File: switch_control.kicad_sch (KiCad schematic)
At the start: 16 parts, among them U10 74LVC1G86, U11 74LVC1G86, U26 74HC00, U27 74LVC1G32

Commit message: Multiplex clock I/O signals
- Allow switching of CLKIN and CLKOUT ports to trigger I/O and other signals
- Add SCT_CLK
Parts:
- U10, U11: Substitution (none) -> TI SN74LVC1G86DCKR
- U27: Substitution (none) -> TI SN74LVC1G32DCKR
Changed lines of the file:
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@@
 			)
 		)
-		(property "Datasheet" "http://www.ti.com/lit/sg/scyt129e/scyt129e.pdf"
+		(property "Datasheet" "https://www.umw-ic.com/static/pdf/f1fd48d5f9832d4f28de5af0ef559744.pdf"
 			(at 154.94 104.14 0)
 			(effects
@@
 		)
 		(property "Part Number" "SN74LVC1G32DCKR"
+			(at 154.94 104.14 0)
+			(effects
+				(font
+					(size 1.27 1.27)
+				)
+				(hide yes)
+			)
+		)
+		(property "Substitution" "TI SN74LVC1G32DCKR"
 			(at 154.94 104.14 0)
 			(effects
@@
 			)
 		)
-		(property "Datasheet" "http://www.ti.com/lit/sg/scyt129e/scyt129e.pdf"
+		(property "Datasheet" "https://www.umw-ic.com/static/pdf/7c3c8f547545258487a86f9b9a30ed55.pdf"
 			(at 154.94 54.61 0)
 			(effects
@@
 		)
 		(property "Part Number" "SN74LVC1G86DCKR"
+			(at 154.94 54.61 0)
+			(effects
+				(font
+					(size 1.27 1.27)
+				)
+				(hide yes)
+			)
+		)
+		(property "Substitution" "TI SN74LVC1G86DCKR"
 			(at 154.94 54.61 0)
 			(effects
@@
 			)
 		)
-		(property "Datasheet" "http://www.ti.com/lit/sg/scyt129e/scyt129e.pdf"
+		(property "Datasheet" "https://www.umw-ic.com/static/pdf/7c3c8f547545258487a86f9b9a30ed55.pdf"
 			(at 161.29 78.74 0)
 			(effects
@@
 			(at 161.29 78.74 0)
 			(effects
+				(font
+					(size 1.27 1.27)
+				)
+				(hide yes)
+			)
+		)
+		(property "Substitution" "TI SN74LVC1G86DCKR"
+			(at 161.29 78.74 0)
+			(effects

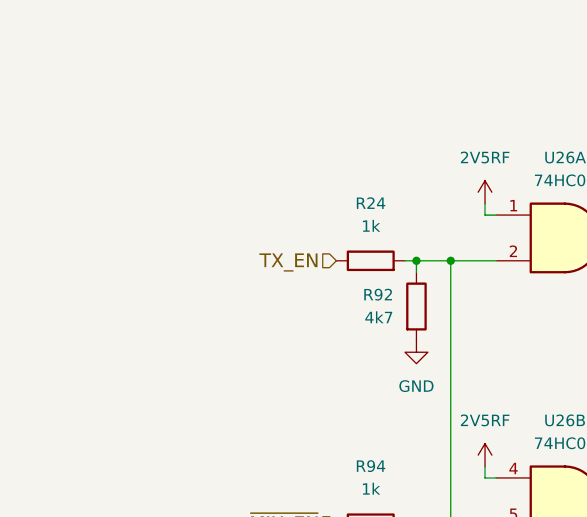
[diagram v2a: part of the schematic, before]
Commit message: Add TX_EN solder jumper
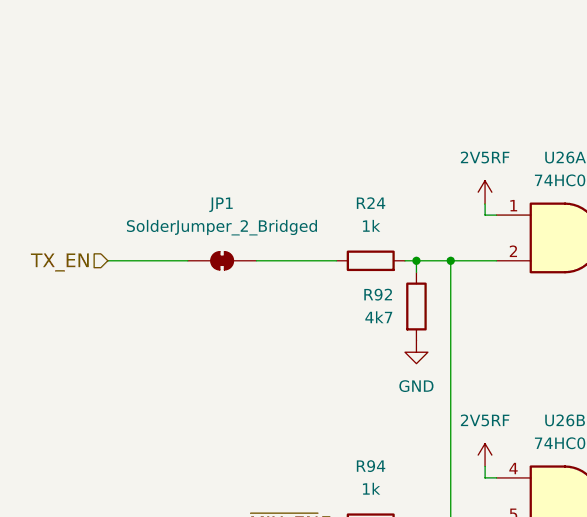
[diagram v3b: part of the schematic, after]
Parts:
- added JP1: SolderJumper_2_Bridged, Jumper:SolderJumper-2_P1.3mm_Bridged_RoundedPad1.0x1.5mm, symbol Jumper:SolderJumper_2_Bridged
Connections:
- net TX_EN: now also JP1.1 (A); no longer R24.1
- new net: JP1.2 (B), R24.1
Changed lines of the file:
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@@
+	(wire
+		(pts
+			(xy 66.04 54.61) (xy 74.93 54.61)
+		)
+		(stroke
+			(width 0)
+			(type default)
+		)
+	)
 	(wire
 		(pts
@@
 		(pts
 			(xy 173.99 34.29) (xy 128.27 34.29)
+		)
+		(stroke
+			(width 0)
+			(type default)
+		)
+	)
+	(wire
+		(pts
+			(xy 82.55 54.61) (xy 91.44 54.61)
 		)
 		(stroke
@@
 	(hierarchical_label "TX_EN"
 		(shape input)
-		(at 91.44 54.61 180)
+		(at 66.04 54.61 180)
 		(effects
 			(font
@@
 				)
 			)
+		)
+	)
+	(symbol
+		(lib_id "Jumper:SolderJumper_2_Bridged")
+		(at 78.74 54.61 0)
+		(unit 1)
+		(exclude_from_sim yes)
+		(in_bom no)
+		(on_board yes)
+		(dnp no)
+		(fields_autoplaced yes)
+		(property "Reference" "JP1"
+			(at 78.74 48.26 0)
+			(effects
+				(font
+					(size 1.27 1.27)
+				)
+			)
+		)
+		(property "Value" "SolderJumper_2_Bridged"
+			(at 78.74 50.8 0)
+			(effects
+				(font
+					(size 1.27 1.27)
+				)
+			)
+		)
+		(property "Footprint" "Jumper:SolderJumper-2_P1.3mm_Bridged_RoundedPad1.0x1.5mm"
+			(at 78.74 54.61 0)
+			(effects
+				(font
+					(size 1.27 1.27)
+				)
+				(hide yes)
+			)
+		)
+		(property "Datasheet" "~"
+			(at 78.74 54.61 0)
+			(effects
+				(font
+					(size 1.27 1.27)
+				)
+				(hide yes)
+			)
+		)
+		(property "Description" "Solder Jumper, 2-pole, closed/bridged"
+			(at 78.74 54.61 0)
+			(effects
+				(font
+					(size 1.27 1.27)
+				)
+				(hide yes)
+			)
+		)
+		(pin "2"
+		)
+		(pin "1"
+		)
+		(instances
+			(project ""
+				(path "/dba4afc6-760f-46cb-a936-032b76448f03/b52297f1-63c0-4931-9c57-b3b41fe2150b"
+					(reference "JP1")
+					(unit 1)
+				)
+			)

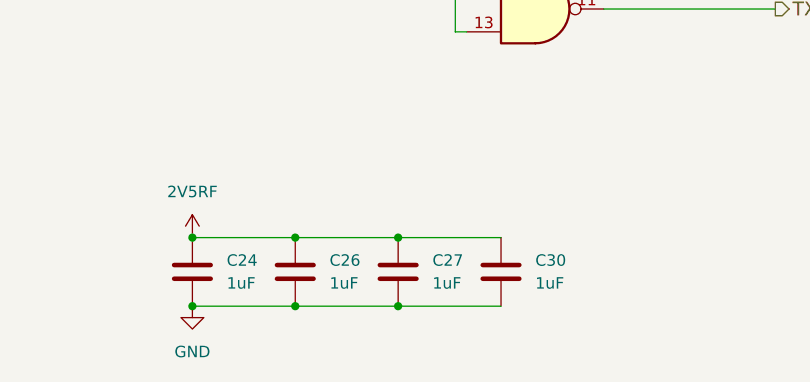
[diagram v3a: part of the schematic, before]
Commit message: Improve power supply filtering and decoupling
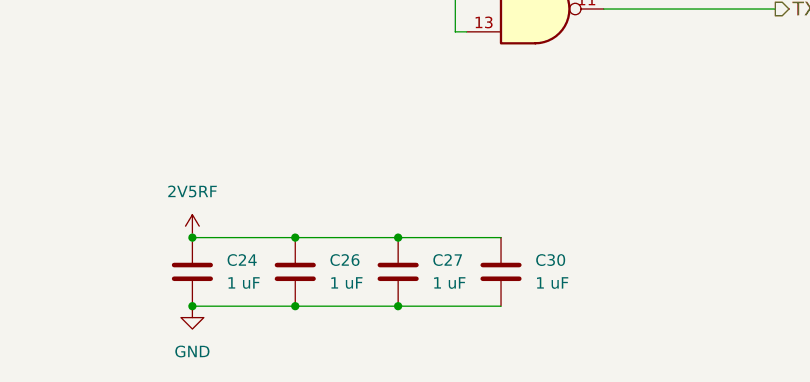
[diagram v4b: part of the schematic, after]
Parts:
- C24, C26, C27, C30: value 1uF -> 1 uF
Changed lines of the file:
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@@
 			)
 		)
-		(property "Value" "1uF"
+		(property "Value" "1 uF"
 			(at 124.46 177.7999 0)
 			(effects
@@
 			)
 		)
-		(property "Value" "1uF"
+		(property "Value" "1 uF"
 			(at 135.89 177.7999 0)
 			(effects
@@
 			)
 		)
-		(property "Value" "1uF"
+		(property "Value" "1 uF"
 			(at 113.03 177.7999 0)
 			(effects
@@
 			)
 		)
-		(property "Value" "1uF"
+		(property "Value" "1 uF"
 			(at 147.32 177.7999 0)
 			(effects

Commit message: Update to KiCad 9
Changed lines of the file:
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@@
 (kicad_sch
-	(version 20231120)
+	(version 20250114)
 	(generator "eeschema")
-	(generator_version "8.0")
+	(generator_version "9.0")
 	(paper "A4")
 	(title_block

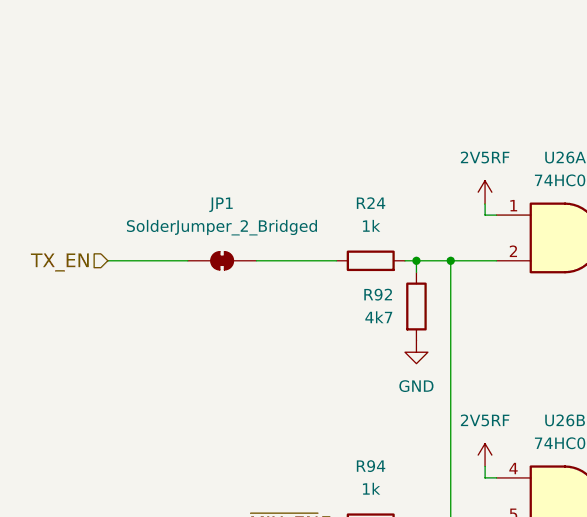
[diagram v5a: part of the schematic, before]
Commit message: Add mixer loss compensation amplifiers
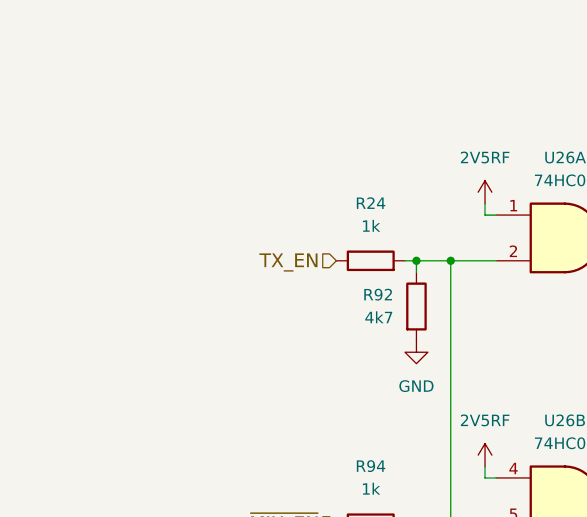
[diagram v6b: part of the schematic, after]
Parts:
- removed JP1: SolderJumper_2_Bridged, Jumper:SolderJumper-2_P1.3mm_Bridged_RoundedPad1.0x1.5mm, symbol Jumper:SolderJumper_2_Bridged
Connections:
- net TX_EN: now also R24.1
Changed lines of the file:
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@@
-	(wire
-		(pts
-			(xy 66.04 54.61) (xy 74.93 54.61)
-		)
-		(stroke
-			(width 0)
-			(type default)
-		)
-	)
 	(wire
 		(pts
@@
 		(pts
 			(xy 173.99 34.29) (xy 128.27 34.29)
-		)
-		(stroke
-			(width 0)
-			(type default)
-		)
-	)
-	(wire
-		(pts
-			(xy 82.55 54.61) (xy 91.44 54.61)
 		)
 		(stroke
@@
 	(hierarchical_label "TX_EN"
 		(shape input)
-		(at 66.04 54.61 180)
+		(at 91.44 54.61 180)
 		(effects
 			(font
@@
 				)
 			)
-		)
-	)
-	(symbol
-		(lib_id "Jumper:SolderJumper_2_Bridged")
-		(at 78.74 54.61 0)
-		(unit 1)
-		(exclude_from_sim yes)
-		(in_bom no)
-		(on_board yes)
-		(dnp no)
-		(fields_autoplaced yes)
-		(property "Reference" "JP1"
-			(at 78.74 48.26 0)
-			(effects
-				(font
-					(size 1.27 1.27)
-				)
-			)
-		)
-		(property "Value" "SolderJumper_2_Bridged"
-			(at 78.74 50.8 0)
-			(effects
-				(font
-					(size 1.27 1.27)
-				)
-			)
-		)
-		(property "Footprint" "Jumper:SolderJumper-2_P1.3mm_Bridged_RoundedPad1.0x1.5mm"
-			(at 78.74 54.61 0)
-			(effects
-				(font
-					(size 1.27 1.27)
-				)
-				(hide yes)
-			)
-		)
-		(property "Datasheet" "~"
-			(at 78.74 54.61 0)
-			(effects
-				(font
-					(size 1.27 1.27)
-				)
-				(hide yes)
-			)
-		)
-		(property "Description" "Solder Jumper, 2-pole, closed/bridged"
-			(at 78.74 54.61 0)
-			(effects
-				(font
-					(size 1.27 1.27)
-				)
-				(hide yes)
-			)
-		)
-		(pin "2"
-		)
-		(pin "1"
-		)
-		(instances
-			(project ""
-				(path "/dba4afc6-760f-46cb-a936-032b76448f03/b52297f1-63c0-4931-9c57-b3b41fe2150b"
-					(reference "JP1")
-					(unit 1)
-				)
-			)

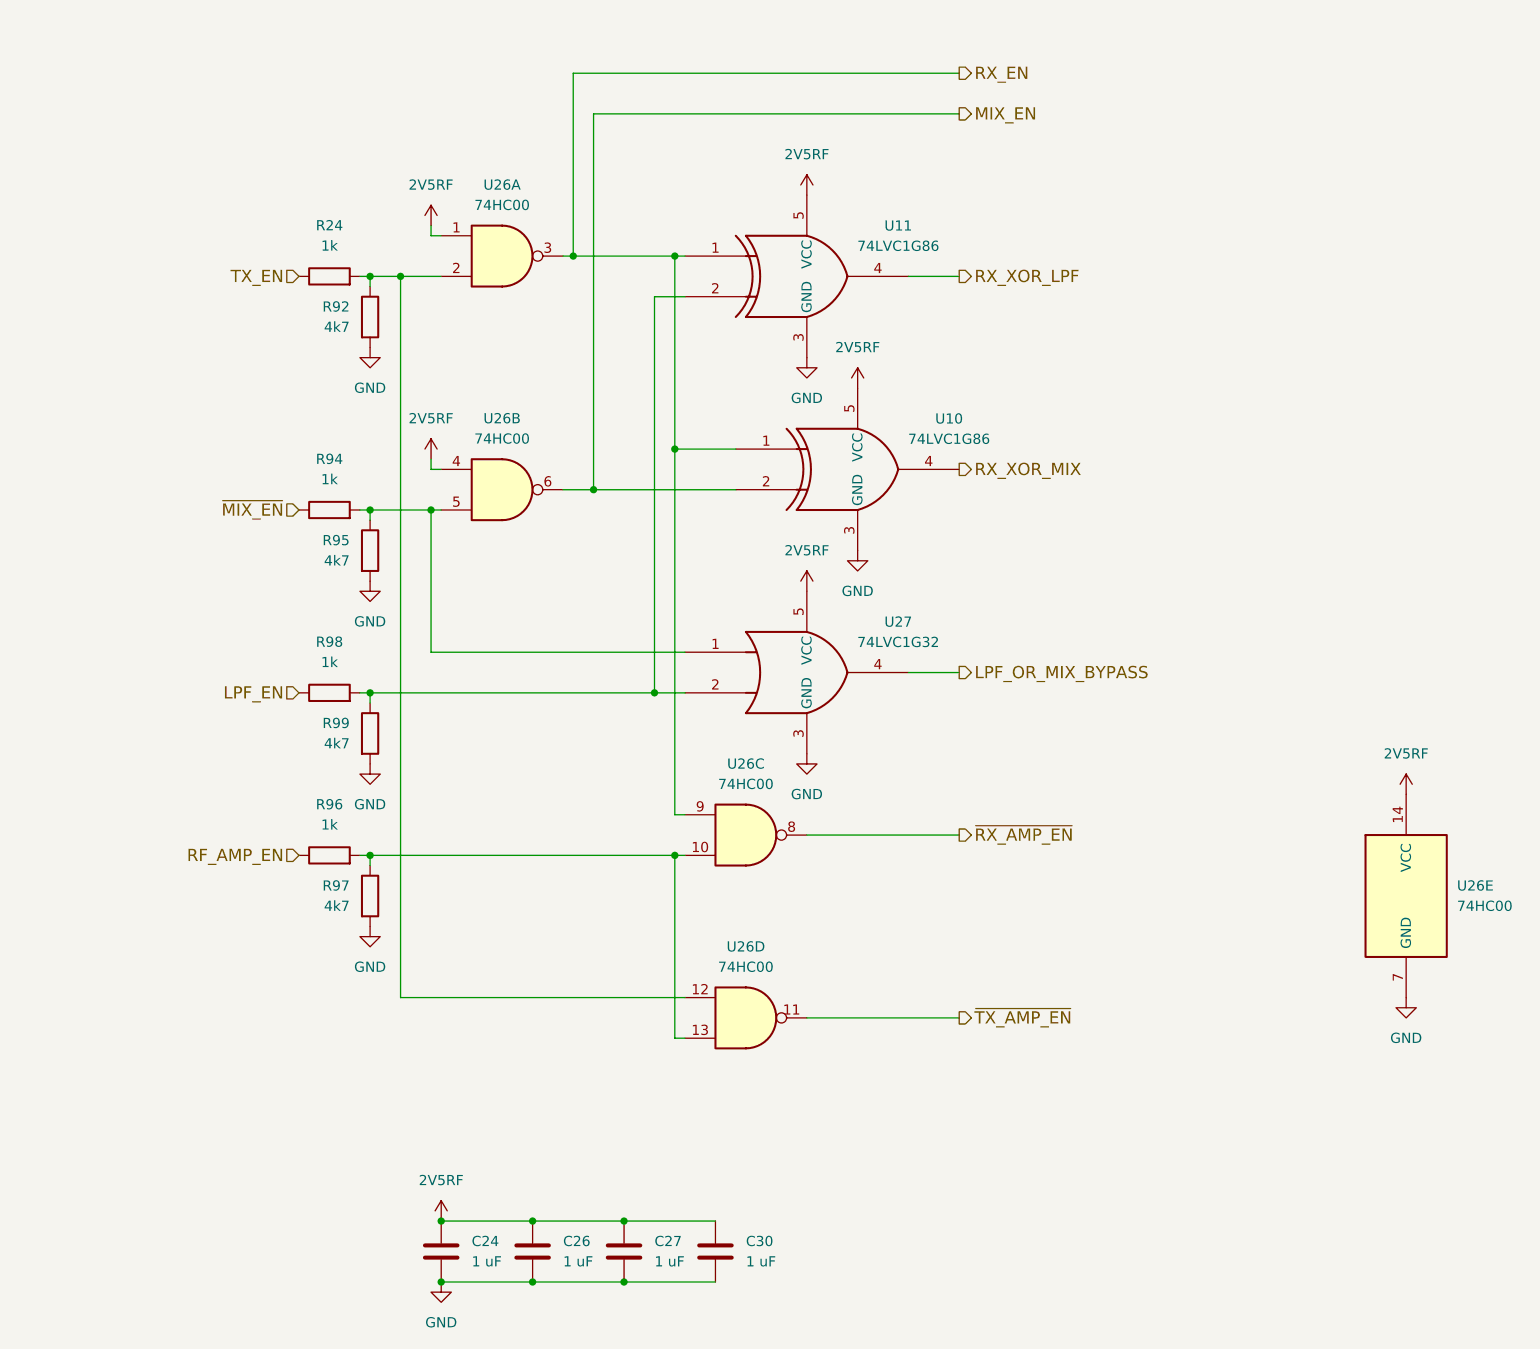
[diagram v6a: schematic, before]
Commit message: Add test points
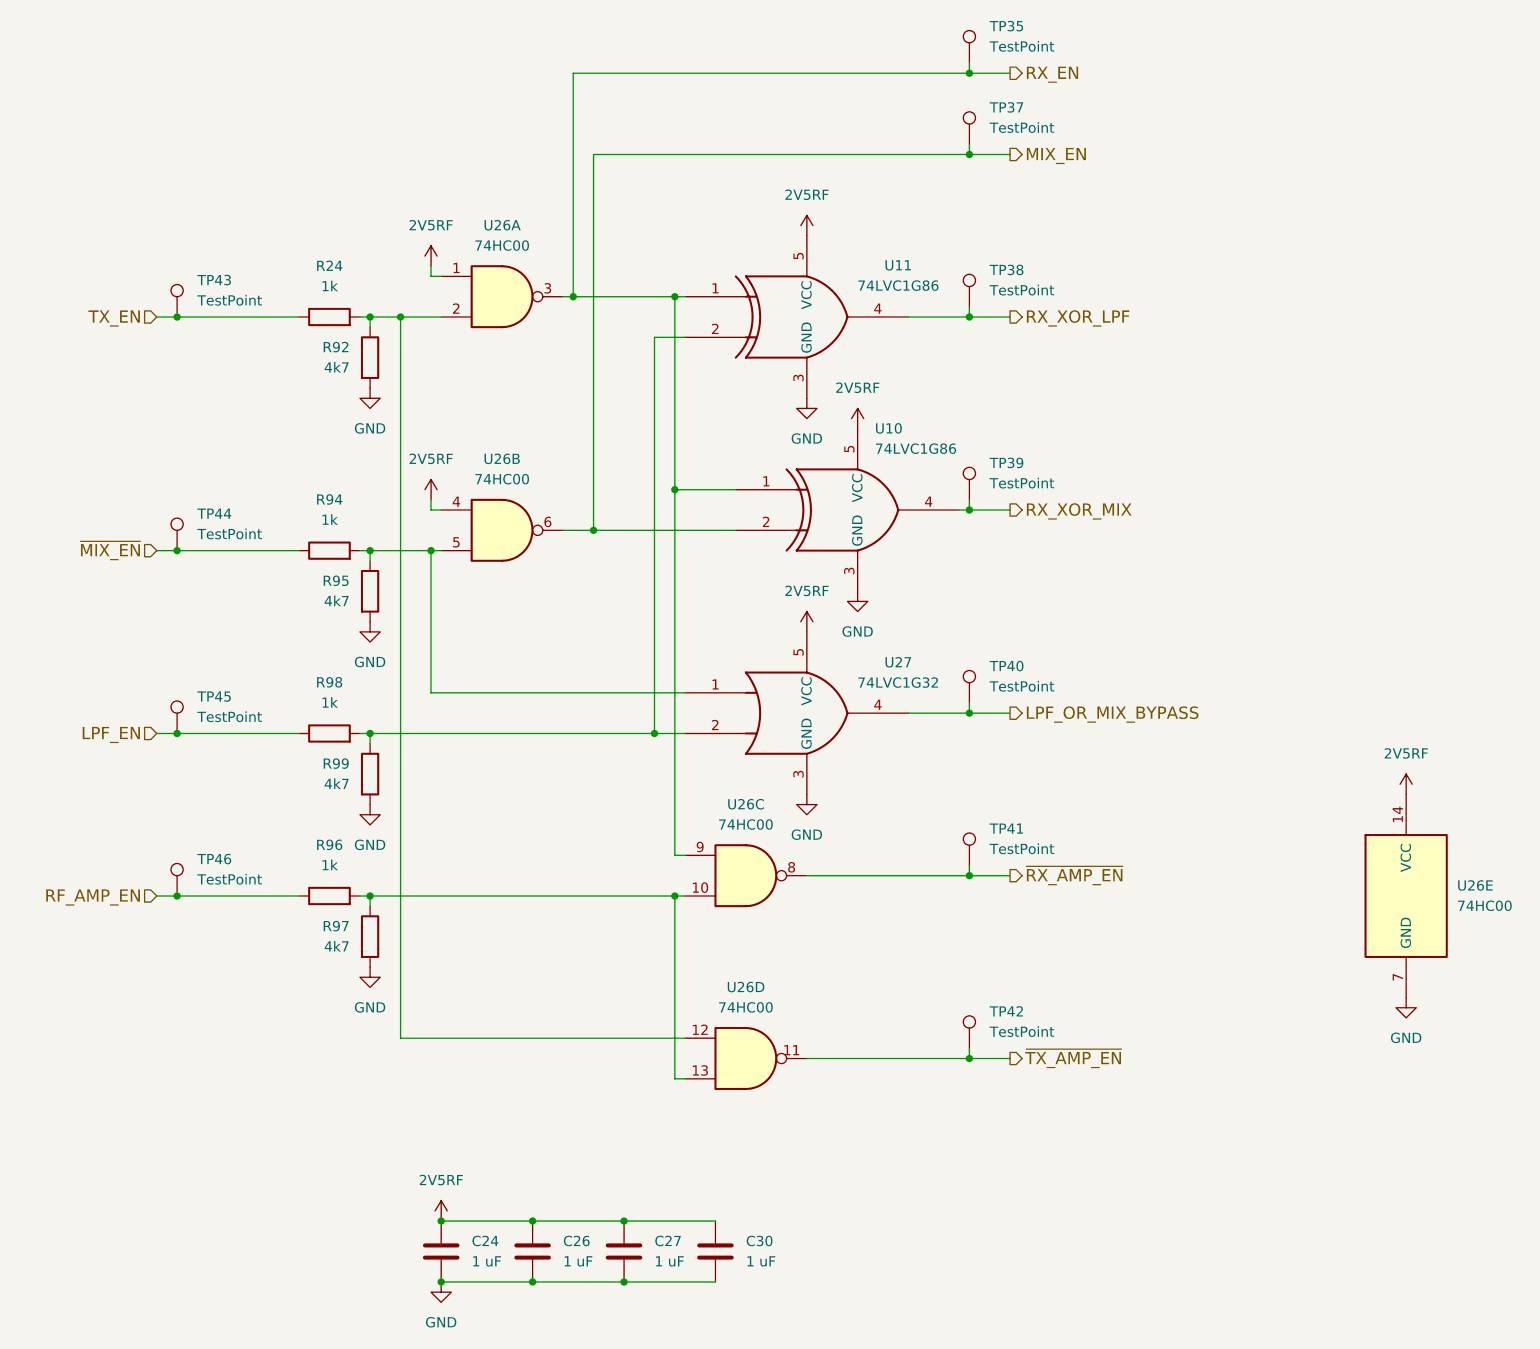
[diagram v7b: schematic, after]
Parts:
- added TP35, TP37, TP38, TP39, TP40, TP41, TP42, TP43, TP44, TP45, TP46: TestPoint, TestPoint:TestPoint_Pad_D1.0mm, symbol Connector:TestPoint
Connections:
- net LPF_EN: now also TP45.1
- net LPF_OR_MIX_BYPASS: now also TP40.1
- net MIX_EN: now also TP37.1
- net RF_AMP_EN: now also TP46.1
- net RX_EN: now also TP35.1
- net RX_XOR_LPF: now also TP38.1
- net RX_XOR_MIX: now also TP39.1
- net TX_EN: now also TP43.1
- net ~{MIX_EN}: now also TP44.1
- net ~{RX_AMP_EN}: now also TP41.1
- net ~{TX_AMP_EN}: now also TP42.1
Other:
- moved on the sheet: R24, R92, R94, R95, R96, R97, R98, R99, U10, U11, U26A, U26B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
